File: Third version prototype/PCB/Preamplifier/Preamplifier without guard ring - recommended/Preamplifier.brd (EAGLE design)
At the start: 130 x 10.5 mm, 63 parts, among them IC1 LTC6268, IC2 LTC6228, T1 CPH3910, X1 87437-0443

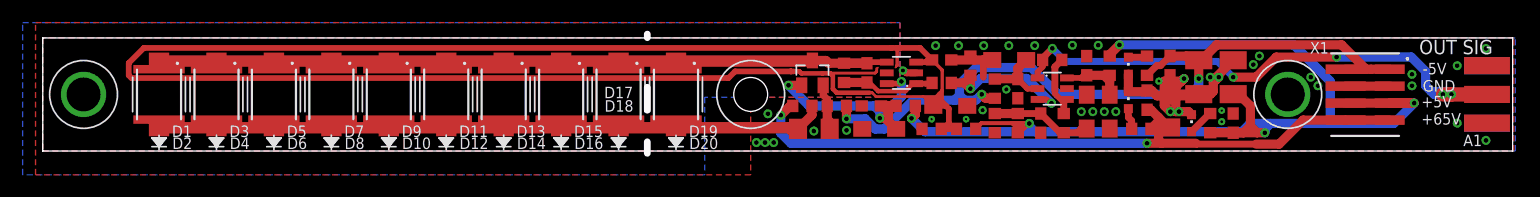
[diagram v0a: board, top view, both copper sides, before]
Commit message: Removed guard ring due to ocurring shorts and adjusted supply rail resistors
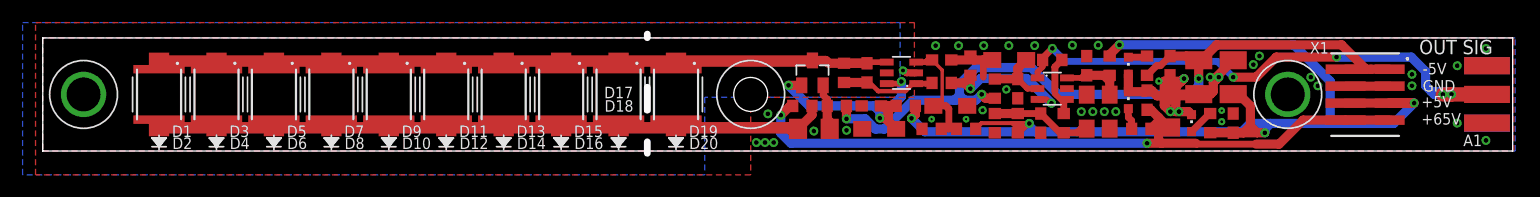
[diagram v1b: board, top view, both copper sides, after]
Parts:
- R10, R11, R9: value 75 -> 1
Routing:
- net N$3: track 173.3 -> 12.6 mm
